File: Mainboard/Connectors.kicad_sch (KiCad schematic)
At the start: 0 parts

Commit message: working mainboard push!
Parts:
- added H1: MountingHole_Pad, MountingHole:MountingHole_2.2mm_M2_Pad_Via, symbol Mechanical:MountingHole_Pad
- added J2, J3: 5745782-6, 57457826:57457826, symbol 5745782-6:5745782-6
- added J4, J5: Conn_01x02_Pin, Connector_PinHeader_2.54mm:PinHeader_1x02_P2.54mm_Vertical, symbol Connector:Conn_01x02_Pin
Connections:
- net 1A_1: now also J3.8
- net 1A_2: now also J3.13
- net 1A_3: now also J3.3
- net 1B_1: now also J3.15
- net 1B_2: now also J3.6
- net 1B_3: now also J3.4
- net 2A_1: now also J3.7
- net 2A_2: now also J3.5
- net 2A_3: now also J3.2
- net 2B_1: now also J3.14
- net 2B_2: now also J3.12
- net 2B_3: now also J3.1
- net AIN+: now also J5.2 (Pin_2)
- net AIN-: now also J5.1 (Pin_1)
- net BIAS: now also J2.7
- net IOUT+: now also J4.2 (Pin_2)
- net IOUT-: now also J4.1 (Pin_1)
- net T_Amp+: now also J2.2
- net T_Amp-: now also J2.1
- net Z+X: now also J2.4
- net Z+Y: now also J2.8
- net Z-X: now also J2.5
- net Z-Y: now also J2.15
- new net +15V: J3.9
- new net -15V: J3.10
- new net GND: J2.10, J2.11, J2.12, J2.13, J2.3, J2.9, J3.11
- new net Shield: H1.1, J2.MH1, J2.MH2, J3.MH1, J3.MH2

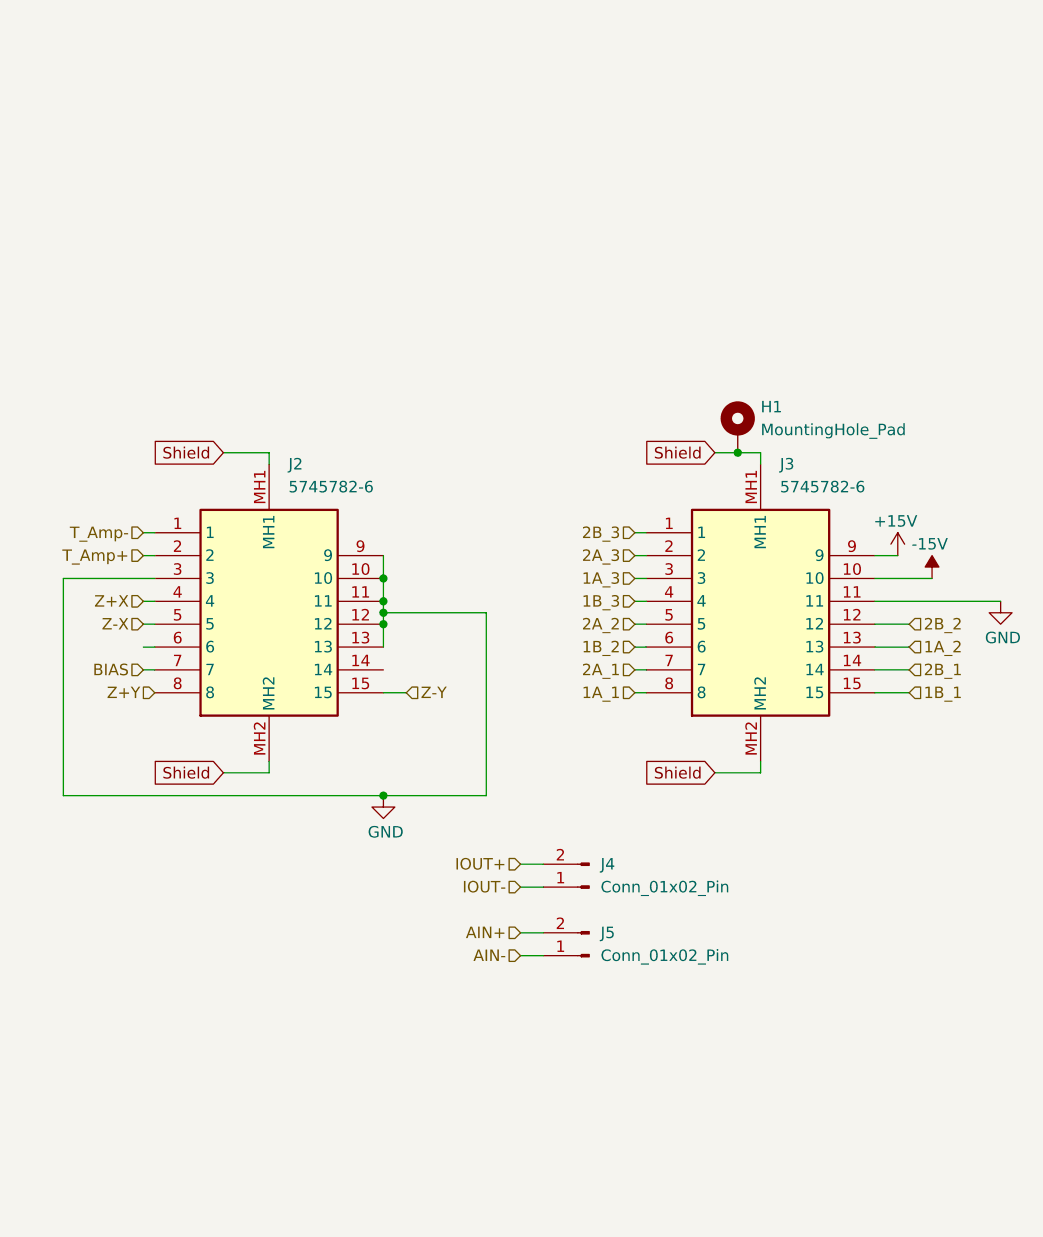
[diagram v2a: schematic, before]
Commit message: mainboard working commits!
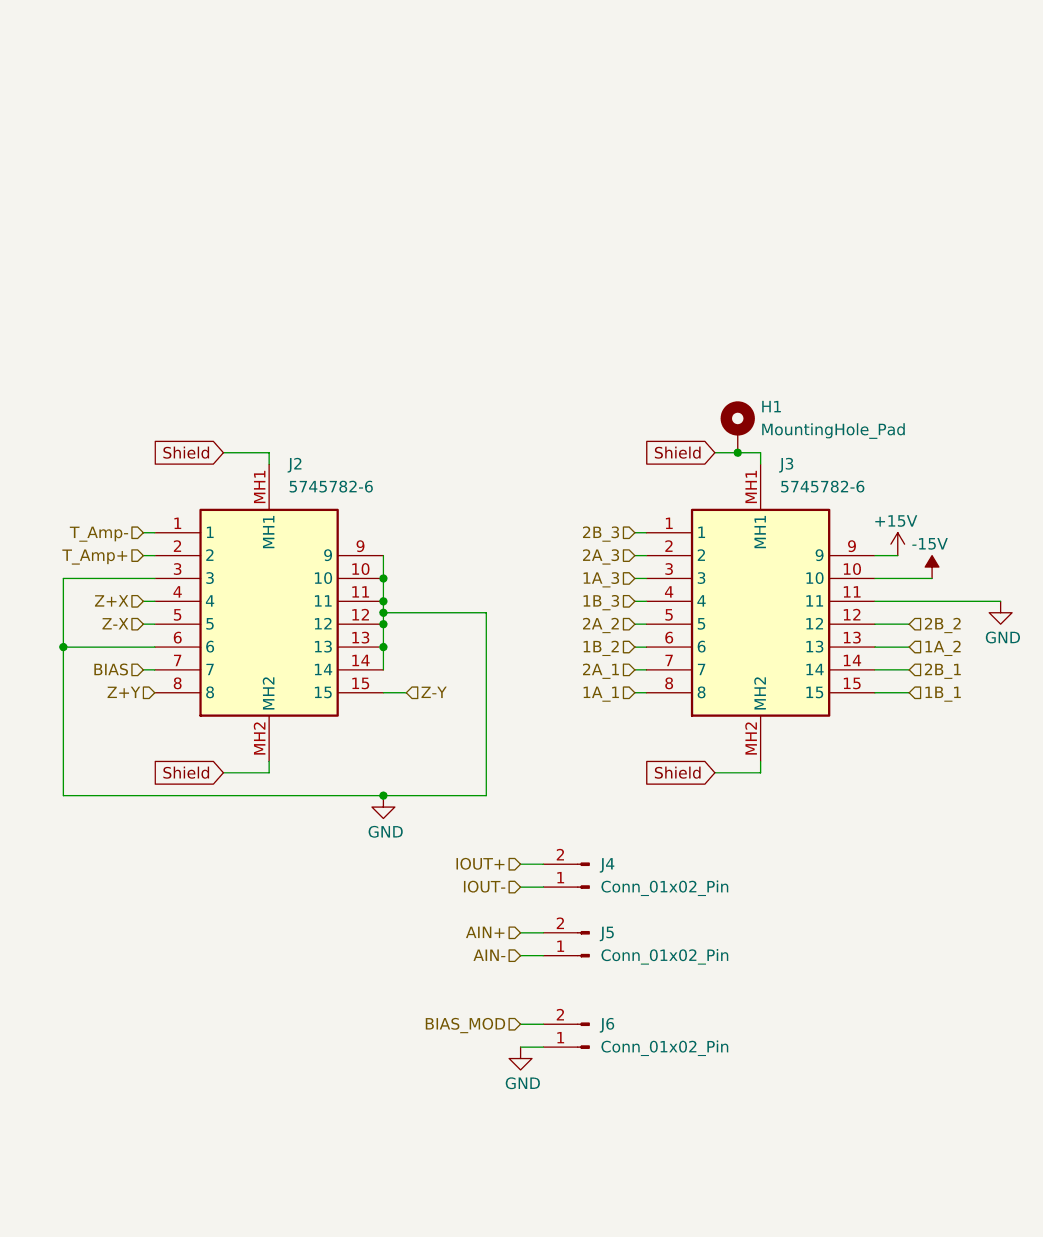
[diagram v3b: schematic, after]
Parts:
- added J6: Conn_01x02_Pin, Connector_PinHeader_2.54mm:PinHeader_1x02_P2.54mm_Vertical, symbol Connector:Conn_01x02_Pin
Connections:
- net GND: now also J2.14, J2.6, J6.1 (Pin_1)
- new net BIAS_MOD: J6.2 (Pin_2)
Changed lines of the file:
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@@
+	)
+	(junction
+		(at 77.47 105.41)
+		(diameter 0)
+		(color 0 0 0 0)
 	)
 	(junction
@@
 	)
 	(junction
+		(at 41.91 105.41)
+		(diameter 0)
+		(color 0 0 0 0)
+	)
+	(junction
 		(at 77.47 121.92)
 		(diameter 0)
@@
 	(wire
 		(pts
+			(xy 41.91 105.41) (xy 41.91 97.79)
+		)
+		(stroke
+			(width 0)
+			(type default)
+		)
+	)
+	(wire
+		(pts
 			(xy 132.08 107.95) (xy 135.89 107.95)
 		)
@@
 	(wire
 		(pts
+			(xy 92.71 149.86) (xy 95.25 149.86)
+		)
+		(stroke
+			(width 0)
+			(type default)
+		)
+	)
+	(wire
+		(pts
 			(xy 50.8 100.33) (xy 52.07 100.33)
 		)
@@
 	(wire
 		(pts
-			(xy 41.91 121.92) (xy 41.91 97.79)
+			(xy 41.91 121.92) (xy 41.91 105.41)
+		)
+		(stroke
+			(width 0)
+			(type default)
+		)
+	)
+	(wire
+		(pts
+			(xy 41.91 105.41) (xy 52.07 105.41)
 		)
 		(stroke
@@
 	(wire
 		(pts
+			(xy 77.47 105.41) (xy 77.47 107.95)
+		)
+		(stroke
+			(width 0)
+			(type default)
+		)
+	)
+	(wire
+		(pts
 			(xy 50.8 95.25) (xy 52.07 95.25)
 		)
@@
 	(wire
 		(pts
-			(xy 50.8 105.41) (xy 52.07 105.41)
-		)
-		(stroke
-			(width 0)
-			(type default)
-		)
-	)
-	(wire
-		(pts
 			(xy 88.9 121.92) (xy 88.9 101.6)
 		)
@@
 		(pts
 			(xy 105.41 110.49) (xy 106.68 110.49)
+		)
+		(stroke
+			(width 0)
+			(type default)
+		)
+	)
+	(wire
+		(pts
+			(xy 92.71 147.32) (xy 95.25 147.32)
 		)
 		(stroke
@@
 		)
 	)
+	(hierarchical_label "BIAS_MOD"
+		(shape input)
+		(at 92.71 147.32 180)
+		(effects
+			(font
+				(size 1.27 1.27)
+			)
+			(justify right)
+		)
+	)
 	(hierarchical_label "2B_1"
 		(shape input)
@@
 			)
 			(justify right)
+		)
+	)
+	(symbol
+		(lib_id "power:GND")
+		(at 92.71 149.86 0)
+		(unit 1)
+		(exclude_from_sim no)
+		(in_bom yes)
+		(on_board yes)
+		(dnp no)
+		(property "Reference" "#PWR093"
+			(at 92.71 156.21 0)
+			(effects
+				(font
+					(size 1.27 1.27)
+				)
+				(hide yes)
+			)
+		)
+		(property "Value" "GND"
+			(at 92.964 153.924 0)
+			(effects
+				(font
+					(size 1.27 1.27)
+				)
+			)
+		)
+		(property "Footprint" ""
+			(at 92.71 149.86 0)
+			(effects
+				(font
+					(size 1.27 1.27)
+				)
+				(hide yes)
+			)
+		)
+		(property "Datasheet" ""
+			(at 92.71 149.86 0)
+			(effects
+				(font
+					(size 1.27 1.27)
+				)
+				(hide yes)
+			)
+		)
+		(property "Description" "Power symbol creates a global label with name \"GND\" , ground"
+			(at 92.71 149.86 0)
+			(effects
+				(font
+					(size 1.27 1.27)
+				)
+				(hide yes)
+			)
+		)
+		(pin "1"
+		)
+		(instances
+			(project "Mainboard"
+				(path "/6062de0a-19b5-4384-b464-187ca20917ea/261a96f3-5d5f-4ec0-8877-95e70d577d88"
+					(reference "#PWR093")
+					(unit 1)
+				)
+			)
 		)
 	)
@@
 					(unit 1)
 				)
+			)
+		)
+	)
+	(symbol
+		(lib_id "Connector:Conn_01x02_Pin")
+		(at 100.33 149.86 180)
+		(unit 1)
+		(exclude_from_sim no)
+		(in_bom yes)
+		(on_board yes)
+		(dnp no)
+		(fields_autoplaced yes)
+		(property "Reference" "J6"
+			(at 101.6 147.3199 0)
+			(effects
+				(font
+					(size 1.27 1.27)
+				)
+				(justify right)
+			)
+		)
+		(property "Value" "Conn_01x02_Pin"
+			(at 101.6 149.8599 0)
+			(effects
+				(font
+					(size 1.27 1.27)
+				)
+				(justify right)
+			)
+		)
+		(property "Footprint" "Connector_PinHeader_2.54mm:PinHeader_1x02_P2.54mm_Vertical"
+			(at 100.33 149.86 0)
+			(effects
+				(font
+					(size 1.27 1.27)
+				)
+				(hide yes)
+			)
+		)
+		(property "Datasheet" "~"
+			(at 100.33 149.86 0)
+			(effects
+				(font
+					(size 1.27 1.27)
+				)
+				(hide yes)
+			)
+		)
+		(property "Description" "Generic connector, single row, 01x02, script generated"
+			(at 100.33 149.86 0)
+			(effects
+				(font
+					(size 1.27 1.27)
+				)
+				(hide yes)
+			)
+		)
+		(pin "2"
+		)
+		(pin "1"
+		)
+		(instances
+			(project "Mainboard"
+				(path "/6062de0a-19b5-4384-b464-187ca20917ea/261a96f3-5d5f-4ec0-8877-95e70d577d88"
+					(reference "J6")
+					(unit 1)
+				)

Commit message: cad update
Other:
- moved on the sheet: J4, J5, J6
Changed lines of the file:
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@@
 	(wire
 		(pts
-			(xy 92.71 137.16) (xy 95.25 137.16)
+			(xy 50.8 134.62) (xy 53.34 134.62)
 		)
 		(stroke
@@
 	(wire
 		(pts
-			(xy 92.71 149.86) (xy 95.25 149.86)
+			(xy 50.8 147.32) (xy 53.34 147.32)
 		)
 		(stroke
@@
 	(wire
 		(pts
-			(xy 92.71 139.7) (xy 95.25 139.7)
+			(xy 50.8 137.16) (xy 53.34 137.16)
 		)
 		(stroke
@@
 	(wire
 		(pts
-			(xy 92.71 132.08) (xy 95.25 132.08)
+			(xy 50.8 129.54) (xy 53.34 129.54)
 		)
 		(stroke
@@
 	(wire
 		(pts
-			(xy 92.71 129.54) (xy 95.25 129.54)
+			(xy 50.8 127) (xy 53.34 127)
 		)
 		(stroke
@@
 	(wire
 		(pts
-			(xy 92.71 147.32) (xy 95.25 147.32)
+			(xy 52.07 144.78) (xy 53.34 144.78)
 		)
 		(stroke
@@
 	(hierarchical_label "AIN-"
 		(shape input)
-		(at 92.71 139.7 180)
+		(at 50.8 137.16 180)
 		(effects
 			(font
@@
 	(hierarchical_label "IOUT-"
 		(shape input)
-		(at 92.71 132.08 180)
+		(at 50.8 129.54 180)
 		(effects
 			(font
@@
 	(hierarchical_label "IOUT+"
 		(shape input)
-		(at 92.71 129.54 180)
+		(at 50.8 127 180)
 		(effects
 			(font
@@
 	(hierarchical_label "AIN+"
 		(shape input)
-		(at 92.71 137.16 180)
+		(at 50.8 134.62 180)
 		(effects
 			(font
@@
 	(hierarchical_label "BIAS_MOD"
 		(shape input)
-		(at 92.71 147.32 180)
+		(at 52.07 144.78 180)
 		(effects
 			(font
@@
 	(symbol
 		(lib_id "power:GND")
-		(at 92.71 149.86 0)
+		(at 50.8 147.32 0)
 		(unit 1)
 		(exclude_from_sim no)
@@
 		(dnp no)
 		(property "Reference" "#PWR093"
-			(at 92.71 156.21 0)
+			(at 50.8 153.67 0)
 			(effects
 				(font
@@
 		)
 		(property "Value" "GND"
-			(at 92.964 153.924 0)
+			(at 51.054 151.384 0)
 			(effects
 				(font
@@
 		)
 		(property "Footprint" ""
-			(at 92.71 149.86 0)
+			(at 50.8 147.32 0)
 			(effects
 				(font
@@
 		)
 		(property "Datasheet" ""
-			(at 92.71 149.86 0)
+			(at 50.8 147.32 0)
 			(effects
 				(font
@@
 		)
 		(property "Description" "Power symbol creates a global label with name \"GND\" , ground"
-			(at 92.71 149.86 0)
+			(at 50.8 147.32 0)
 			(effects
 				(font
@@
 	(symbol
 		(lib_id "Connector:Conn_01x02_Pin")
-		(at 100.33 132.08 180)
+		(at 58.42 129.54 180)
 		(unit 1)
 		(exclude_from_sim no)
@@
 		(fields_autoplaced yes)
 		(property "Reference" "J4"
-			(at 101.6 129.5399 0)
+			(at 59.69 126.9999 0)
 			(effects
 				(font
@@
 		)
 		(property "Value" "Conn_01x02_Pin"
-			(at 101.6 132.0799 0)
+			(at 59.69 129.5399 0)
 			(effects
 				(font
@@
 		)
 		(property "Footprint" "Connector_PinHeader_2.54mm:PinHeader_1x02_P2.54mm_Vertical"
-			(at 100.33 132.08 0)
+			(at 58.42 129.54 0)
 			(effects
 				(font
@@
 		)
 		(property "Datasheet" "~"
-			(at 100.33 132.08 0)
+			(at 58.42 129.54 0)
 			(effects
 				(font
@@
 		)
 		(property "Description" "Generic connector, single row, 01x02, script generated"
-			(at 100.33 132.08 0)
+			(at 58.42 129.54 0)
 			(effects
 				(font
@@
 	(symbol
 		(lib_id "Connector:Conn_01x02_Pin")
-		(at 100.33 139.7 180)
+		(at 58.42 137.16 180)
 		(unit 1)
 		(exclude_from_sim no)
@@
 		(fields_autoplaced yes)
 		(property "Reference" "J5"
-			(at 101.6 137.1599 0)
+			(at 59.69 134.6199 0)
 			(effects
 				(font
@@
 		)
 		(property "Value" "Conn_01x02_Pin"
-			(at 101.6 139.6999 0)
+			(at 59.69 137.1599 0)
 			(effects
 				(font
@@
 		)
 		(property "Footprint" "Connector_PinHeader_2.54mm:PinHeader_1x02_P2.54mm_Vertical"
-			(at 100.33 139.7 0)
+			(at 58.42 137.16 0)
 			(effects
 				(font
@@
 		)
 		(property "Datasheet" "~"
-			(at 100.33 139.7 0)
+			(at 58.42 137.16 0)
 			(effects
 				(font
@@
 		)
 		(property "Description" "Generic connector, single row, 01x02, script generated"
-			(at 100.33 139.7 0)
+			(at 58.42 137.16 0)
 			(effects
 				(font
@@
 	(symbol
 		(lib_id "Connector:Conn_01x02_Pin")
-		(at 100.33 149.86 180)
+		(at 58.42 147.32 180)
 		(unit 1)
 		(exclude_from_sim no)
@@
 		(fields_autoplaced yes)
 		(property "Reference" "J6"
-			(at 101.6 147.3199 0)
+			(at 59.69 144.7799 0)
 			(effects
 				(font
@@
 		)
 		(property "Value" "Conn_01x02_Pin"
-			(at 101.6 149.8599 0)
+			(at 59.69 147.3199 0)
 			(effects
 				(font
@@
 		)
 		(property "Footprint" "Connector_PinHeader_2.54mm:PinHeader_1x02_P2.54mm_Vertical"
-			(at 100.33 149.86 0)
+			(at 58.42 147.32 0)
 			(effects
 				(font
@@
 		)
 		(property "Datasheet" "~"
-			(at 100.33 149.86 0)
+			(at 58.42 147.32 0)
 			(effects
 				(font
@@
 		)
 		(property "Description" "Generic connector, single row, 01x02, script generated"
-			(at 100.33 149.86 0)
-			(effects
-				(font
+			(at 58.42 147.32 0)
+			(effects
+				(font
